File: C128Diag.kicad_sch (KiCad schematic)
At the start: 60 parts, among them J1 CP1, J2 CP2, J3 KB, J4 Cas, J5 Aud, J6 Serial, J7 UP, P1 1k, U1 4066, U10 74LS04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

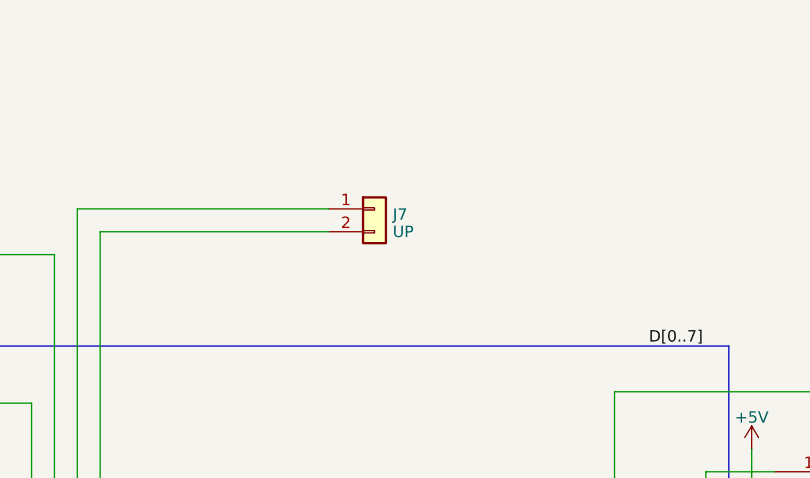
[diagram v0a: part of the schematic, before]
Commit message: Added missing user port connector wiring, fixes #1.
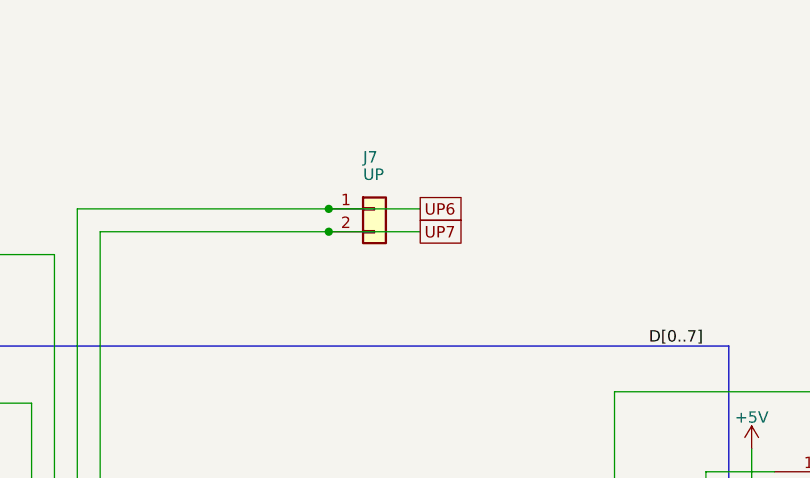
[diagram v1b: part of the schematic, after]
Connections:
- net UP6: now reaches J7.1 (Pin_1), U10.13, U7.4
- net UP7: now reaches J7.2 (Pin_2), U11.11, U8.10
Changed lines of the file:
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@@
   (junction (at 335.28 104.14) (diameter 0) (color 0 0 0 0)
   )
+  (junction (at 306.07 34.29) (diameter 0) (color 0 0 0 0)
+  )
   (junction (at 275.59 80.01) (diameter 0) (color 0 0 0 0)
   )
@@
   (junction (at 27.94 170.18) (diameter 0) (color 0 0 0 0)
   )
+  (junction (at 306.07 36.83) (diameter 0) (color 0 0 0 0)
+  )
   (junction (at 223.52 196.85) (diameter 0) (color 0 0 0 0)
   )
@@
     (stroke (width 0) (type default))
   )
+  (wire (pts (xy 306.07 34.29) (xy 316.23 34.29))
+    (stroke (width 0) (type default))
+  )
   (wire (pts (xy 353.06 106.68) (xy 355.6 106.68))
     (stroke (width 0) (type default))
@@
     (stroke (width 0) (type default))
   )
+  (wire (pts (xy 306.07 36.83) (xy 316.23 36.83))
+    (stroke (width 0) (type default))
+  )
   (wire (pts (xy 321.31 176.53) (xy 313.69 176.53))
     (stroke (width 0) (type default))
@@
     )
   )
+  (global_label "UP7" (shape passive) (at 316.23 36.83 0) (fields_autoplaced)
+    (effects (font (size 1.27 1.27)) (justify left))
+    (property "Intersheetrefs" "${INTERSHEET_REFS}" (at 321.9139 36.83 0)
+      (effects (font (size 1.27 1.27)) (justify left) hide)
+    )
+  )
   (global_label "CP1_6" (shape passive) (at 20.32 46.99 180) (fields_autoplaced)
     (effects (font (size 1.27 1.27)) (justify right))
@@
     )
   )
+  (global_label "UP6" (shape passive) (at 316.23 34.29 0) (fields_autoplaced)
+    (effects (font (size 1.27 1.27)) (justify left))
+    (property "Intersheetrefs" "${INTERSHEET_REFS}" (at 321.9139 34.29 0)
+      (effects (font (size 1.27 1.27)) (justify left) hide)
+    )
+  )
   (global_label "KB1" (shape passive) (at 20.32 175.26 180) (fields_autoplaced)
     (effects (font (size 1.27 1.27)) (justify right))
@@
   )
   (symbol (lib_id "Connector_Generic:Conn_01x02") (at 311.15 34.29 0) (unit 1)
-    (in_bom yes) (on_board yes) (dnp no) (fields_autoplaced)
-    (property "Reference" "J7" (at 313.182 34.9163 0)
+    (in_bom yes) (on_board yes) (dnp no)
+    (property "Reference" "J7" (at 309.88 28.559 0)
       (effects (font (size 1.27 1.27)) (justify left))
     )
-    (property "Value" "UP" (at 313.182 36.8373 0)
+    (property "Value" "UP" (at 309.88 30.48 0)
       (effects (font (size 1.27 1.27)) (justify left))
     )
